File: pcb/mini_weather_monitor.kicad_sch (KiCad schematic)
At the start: 25 parts, among them J1 Conn_01x02, Q1 IRLML6402, U2 4.0inch_SPI_MSP4021, U2_BME280 module_bme280, U3_BH1750 module_bh1750

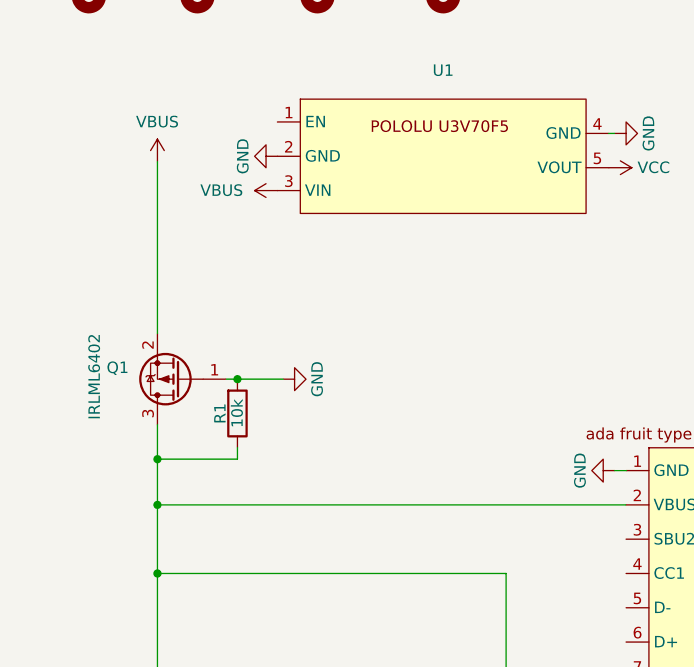
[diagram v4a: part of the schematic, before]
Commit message: fixing mosfet setup, also updating for day of the week length
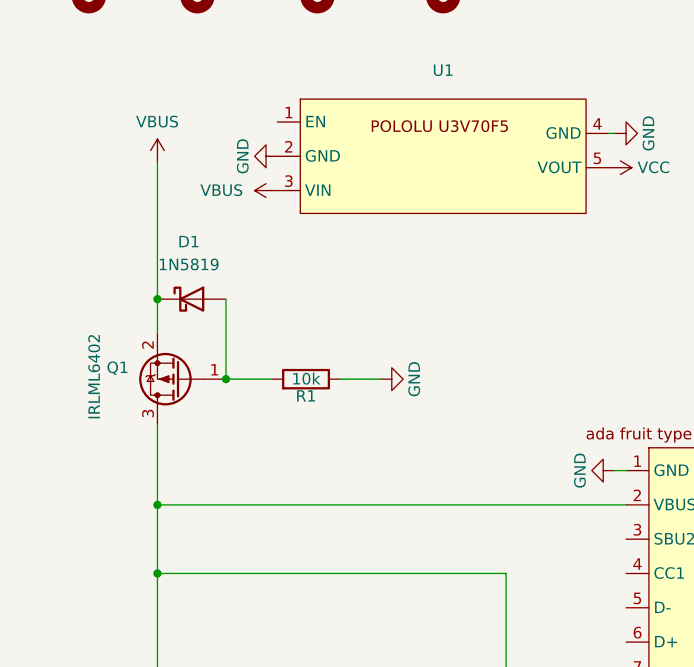
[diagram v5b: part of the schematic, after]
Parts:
- added D1: 1N5819, Diode_SMD:D_SOD-123, symbol Diode:1N5819
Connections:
- net GND: now also R1.1; no longer Q1.1 (G), R1.2
- net VBUS: now also D1.1 (K)
- net at Q1.3 (D), adafruit_type_c_breakout_rev_b1.2 (VBUS), adafruit_type_c_vertical_breakout1.10 (VBUS)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: no longer R1.1
- new net: D1.2 (A), Q1.1 (G), R1.2
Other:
- moved on the sheet: R1
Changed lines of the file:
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@@
+	)
+	(junction
+		(at 27.94 58.42)
+		(diameter 0)
+		(color 0 0 0 0)
 	)
 	(junction
@@
 	)
 	(junction
-		(at 27.94 76.2)
-		(diameter 0)
-		(color 0 0 0 0)
-	)
-	(junction
 		(at 253.365 91.44)
 		(diameter 0)
@@
 	)
 	(junction
+		(at 35.56 67.31)
+		(diameter 0)
+		(color 0 0 0 0)
+	)
+	(junction
 		(at 100.33 117.475)
 		(diameter 0)
@@
 	)
 	(junction
-		(at 36.83 67.31)
-		(diameter 0)
-		(color 0 0 0 0)
-	)
-	(junction
 		(at 196.85 55.245)
 		(diameter 0)
@@
 	(wire
 		(pts
-			(xy 27.94 43.18) (xy 27.94 62.23)
+			(xy 27.94 43.18) (xy 27.94 58.42)
 		)
 		(stroke
@@
 	(wire
 		(pts
+			(xy 35.56 58.42) (xy 35.56 67.31)
+		)
+		(stroke
+			(width 0)
+			(type default)
+		)
+	)
+	(wire
+		(pts
 			(xy 182.88 73.025) (xy 182.88 102.235)
 		)
@@
 	(wire
 		(pts
-			(xy 27.94 72.39) (xy 27.94 76.2)
+			(xy 27.94 72.39) (xy 27.94 81.28)
 		)
 		(stroke
@@
 	(wire
 		(pts
-			(xy 41.91 67.31) (xy 36.83 67.31)
-		)
-		(stroke
-			(width 0)
-			(type default)
-		)
-	)
-	(wire
-		(pts
 			(xy 248.285 35.56) (xy 248.285 77.47)
 		)
@@
 	(wire
 		(pts
-			(xy 36.83 67.31) (xy 35.56 67.31)
+			(xy 35.56 67.31) (xy 40.64 67.31)
 		)
 		(stroke
@@
 	(wire
 		(pts
+			(xy 27.94 58.42) (xy 27.94 62.23)
+		)
+		(stroke
+			(width 0)
+			(type default)
+		)
+	)
+	(wire
+		(pts
 			(xy 190.5 97.155) (xy 194.31 97.155)
 		)
@@
 	(wire
 		(pts
-			(xy 27.94 76.2) (xy 27.94 81.28)
-		)
-		(stroke
-			(width 0)
-			(type default)
-		)
-	)
-	(wire
-		(pts
 			(xy 205.105 60.325) (xy 179.07 60.325)
 		)
@@
 	(wire
 		(pts
-			(xy 36.83 76.2) (xy 27.94 76.2)
-		)
-		(stroke
-			(width 0)
-			(type default)
-		)
-	)
-	(wire
-		(pts
 			(xy 121.92 81.915) (xy 125.73 81.915)
 		)
@@
 	(wire
 		(pts
-			(xy 36.83 74.93) (xy 36.83 76.2)
-		)
-		(stroke
-			(width 0)
-			(type default)
-		)
-	)
-	(wire
-		(pts
 			(xy 156.21 46.355) (xy 158.75 46.355)
 		)
@@
 		(pts
 			(xy 95.885 112.395) (xy 100.33 112.395)
+		)
+		(stroke
+			(width 0)
+			(type default)
+		)
+	)
+	(wire
+		(pts
+			(xy 48.26 67.31) (xy 52.705 67.31)
 		)
 		(stroke
@@
 	(symbol
 		(lib_id "power:GND")
-		(at 41.91 67.31 90)
+		(at 52.705 67.31 90)
 		(unit 1)
 		(exclude_from_sim no)
@@
 		(dnp no)
 		(property "Reference" "#PWR015"
-			(at 48.26 67.31 0)
+			(at 59.055 67.31 0)
 			(effects
 				(font
@@
 		)
 		(property "Value" "GND"
-			(at 45.72 67.31 0)
+			(at 56.515 67.31 0)
 			(effects
 				(font
@@
 		)
 		(property "Footprint" ""
-			(at 41.91 67.31 0)
+			(at 52.705 67.31 0)
 			(effects
 				(font
@@
 		)
 		(property "Datasheet" ""
-			(at 41.91 67.31 0)
+			(at 52.705 67.31 0)
 			(effects
 				(font
@@
 		)
 		(property "Description" ""
-			(at 41.91 67.31 0)
+			(at 52.705 67.31 0)
 			(effects
 				(font
@@
 	(symbol
 		(lib_id "Device:R")
-		(at 36.83 71.12 0)
+		(at 44.45 67.31 270)
 		(mirror x)
 		(unit 1)
@@
 		(dnp no)
 		(property "Reference" "R1"
-			(at 34.925 71.12 90)
+			(at 44.45 69.215 90)
 			(effects
 				(font
@@
 		)
 		(property "Value" "10k"
-			(at 36.83 71.12 90)
+			(at 44.45 67.31 90)
 			(effects
 				(font
@@
 		)
 		(property "Footprint" "Resistor_SMD:R_1206_3216Metric"
-			(at 35.052 71.12 90)
+			(at 44.45 69.088 90)
 			(effects
 				(font
@@
 		)
 		(property "Datasheet" "~"
-			(at 36.83 71.12 0)
+			(at 44.45 67.31 0)
 			(effects
 				(font
@@
 		)
 		(property "Description" "Resistor"
-			(at 36.83 71.12 0)
+			(at 44.45 67.31 0)
 			(effects
 				(font
@@
 					(unit 1)
 				)
+			)
+		)
+	)
+	(symbol
+		(lib_id "Diode:1N5819")
+		(at 31.75 58.42 0)
+		(unit 1)
+		(exclude_from_sim no)
+		(in_bom yes)
+		(on_board yes)
+		(dnp no)
+		(fields_autoplaced yes)
+		(property "Reference" "D1"
+			(at 31.4325 52.07 0)
+			(effects
+				(font
+					(size 1.27 1.27)
+				)
+			)
+		)
+		(property "Value" "1N5819"
+			(at 31.4325 54.61 0)
+			(effects
+				(font
+					(size 1.27 1.27)
+				)
+			)
+		)
+		(property "Footprint" "Diode_SMD:D_SOD-123"
+			(at 31.75 62.865 0)
+			(effects
+				(font
+					(size 1.27 1.27)
+				)
+				(hide yes)
+			)
+		)
+		(property "Datasheet" "http://www.vishay.com/docs/88525/1n5817.pdf"
+			(at 31.75 58.42 0)
+			(effects
+				(font
+					(size 1.27 1.27)
+				)
+				(hide yes)
+			)
+		)
+		(property "Description" "40V 1A Schottky Barrier Rectifier Diode, DO-41"
+			(at 31.75 58.42 0)
+			(effects
+				(font
+					(size 1.27 1.27)
+				)
+				(hide yes)
+			)
+		)
+		(pin "1"
+		)
+		(pin "2"
+		)
+		(instances
+			(project "mini_weather_monitor"
+				(path "/e63e39d7-6ac0-4ffd-8aa3-1841a4541b55"
+					(reference "D1")
+					(unit 1)
+				)

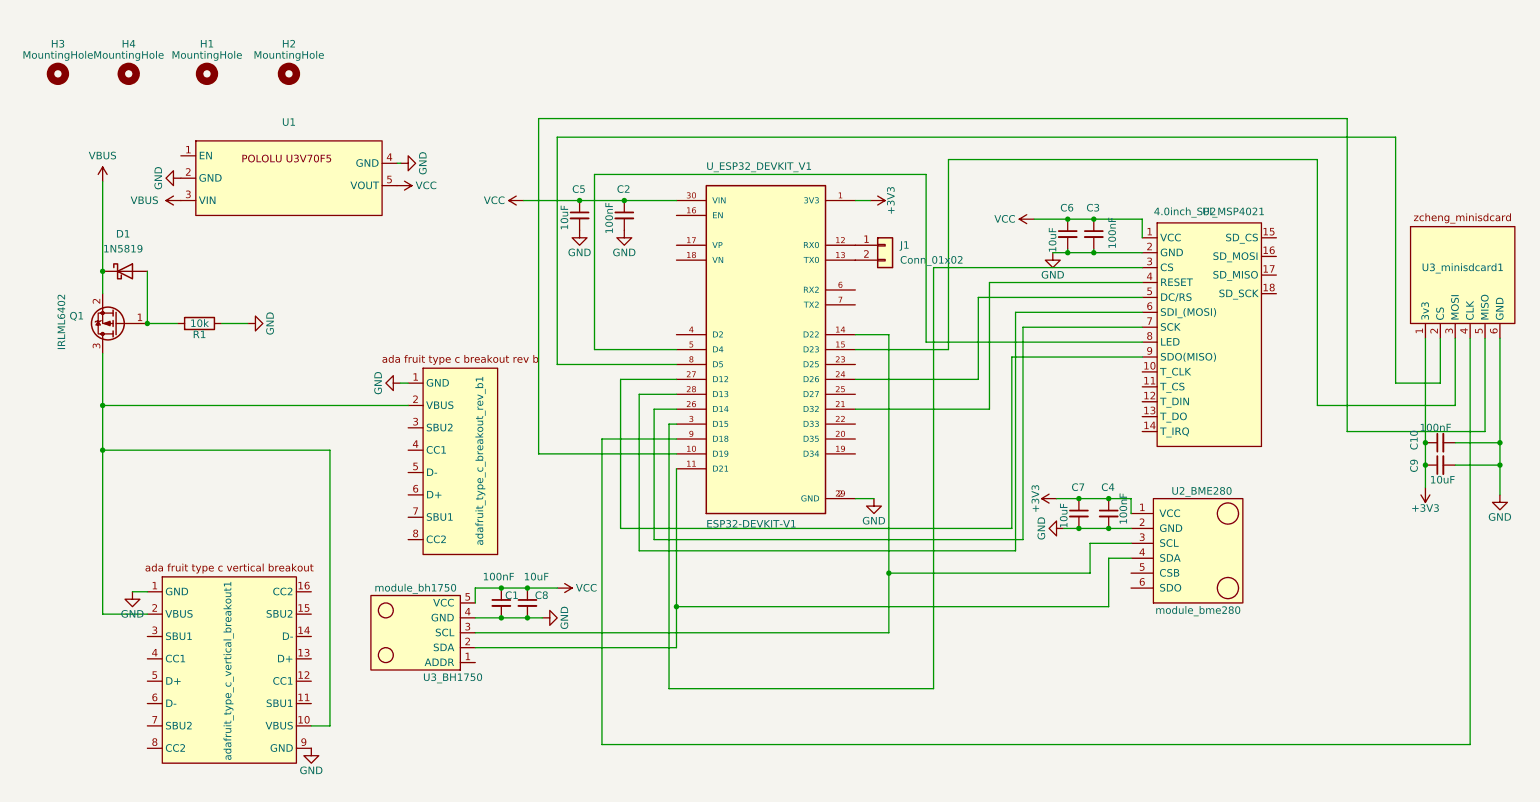
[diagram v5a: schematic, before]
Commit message: adding passthrough
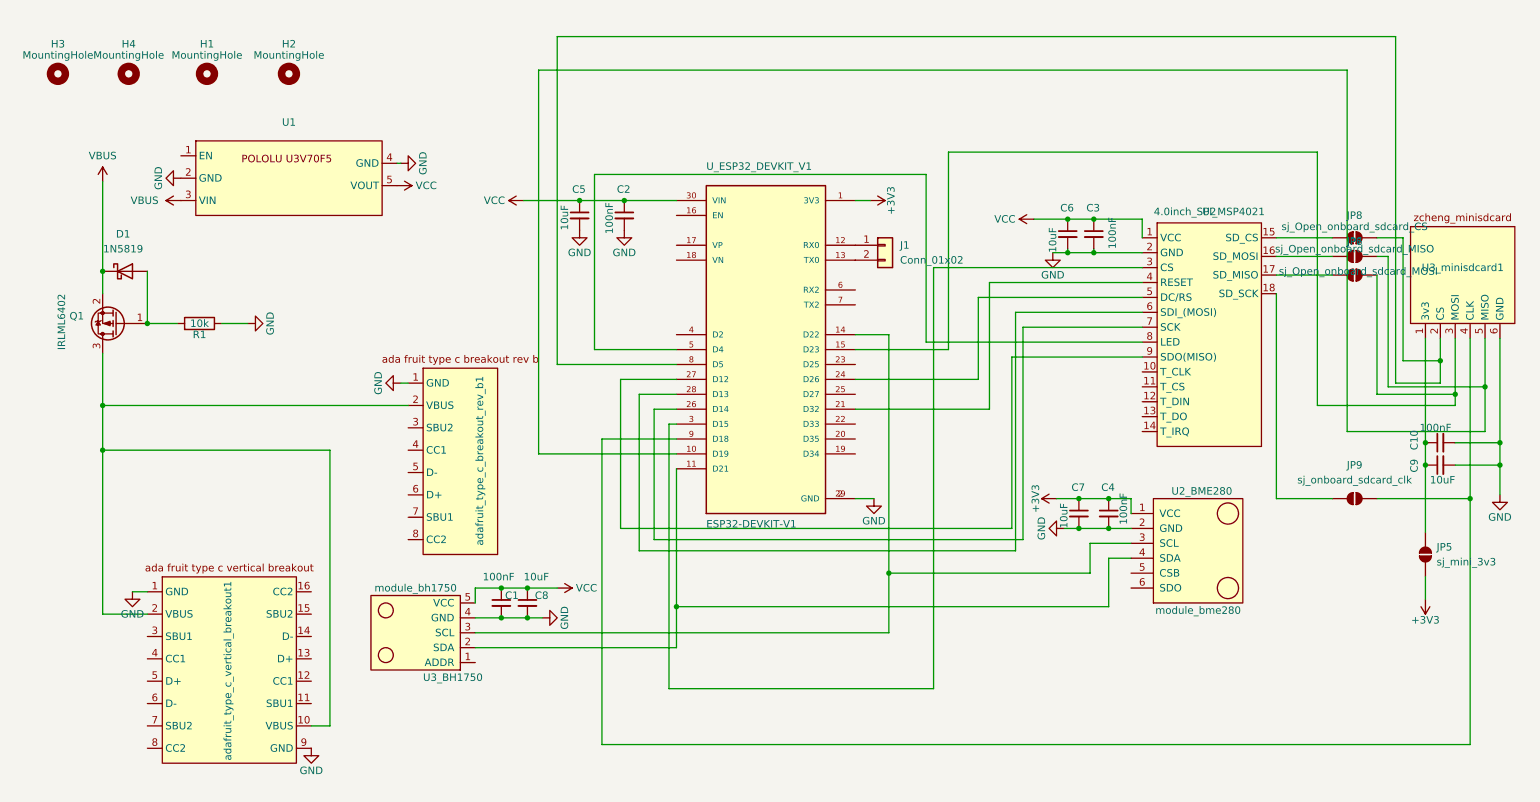
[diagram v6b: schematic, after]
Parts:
- added JP5: sj_mini_3v3, Jumper:SolderJumper-2_P1.3mm_Open_RoundedPad1.0x1.5mm, symbol Jumper:SolderJumper_2_Open
- added JP6: sj_Open_onboard_sdcard_MOSI, Jumper:SolderJumper-2_P1.3mm_Open_RoundedPad1.0x1.5mm, symbol Jumper:SolderJumper_2_Open
- added JP7: sj_Open_onboard_sdcard_MISO, Jumper:SolderJumper-2_P1.3mm_Open_RoundedPad1.0x1.5mm, symbol Jumper:SolderJumper_2_Open
- added JP8: sj_Open_onboard_sdcard_CS, Jumper:SolderJumper-2_P1.3mm_Open_RoundedPad1.0x1.5mm, symbol Jumper:SolderJumper_2_Open
- added JP9: sj_onboard_sdcard_clk, Jumper:SolderJumper-2_P1.3mm_Open_RoundedPad1.0x1.5mm, symbol Jumper:SolderJumper_2_Open
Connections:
- net +3V3: now also JP5.1 (A); no longer C10.1, C9.1, U3_minisdcard1.1 (3v3)
- net at U2.15 (SD_CS): now also JP8.1 (A)
- net at U2.16 (SD_MOSI): now also JP6.1 (A)
- net at U2.17 (SD_MISO): now also JP7.1 (A)
- net at U2.18 (SD_SCK): now also JP9.1 (A)
- net at U3_minisdcard1.5 (MISO), U_ESP32_DEVKIT_V1.10 (D19): now also JP6.2 (B)
- net at U3_minisdcard1.3 (MOSI), U_ESP32_DEVKIT_V1.15 (D23): now also JP7.2 (B)
- net at U3_minisdcard1.2 (CS), U_ESP32_DEVKIT_V1.8 (D5): now also JP8.2 (B)
- net at U3_minisdcard1.4 (CLK), U_ESP32_DEVKIT_V1.9 (D18): now also JP9.2 (B)
- new net: C10.1, C9.1, JP5.2 (B), U3_minisdcard1.1 (3v3)

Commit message: slight retrace
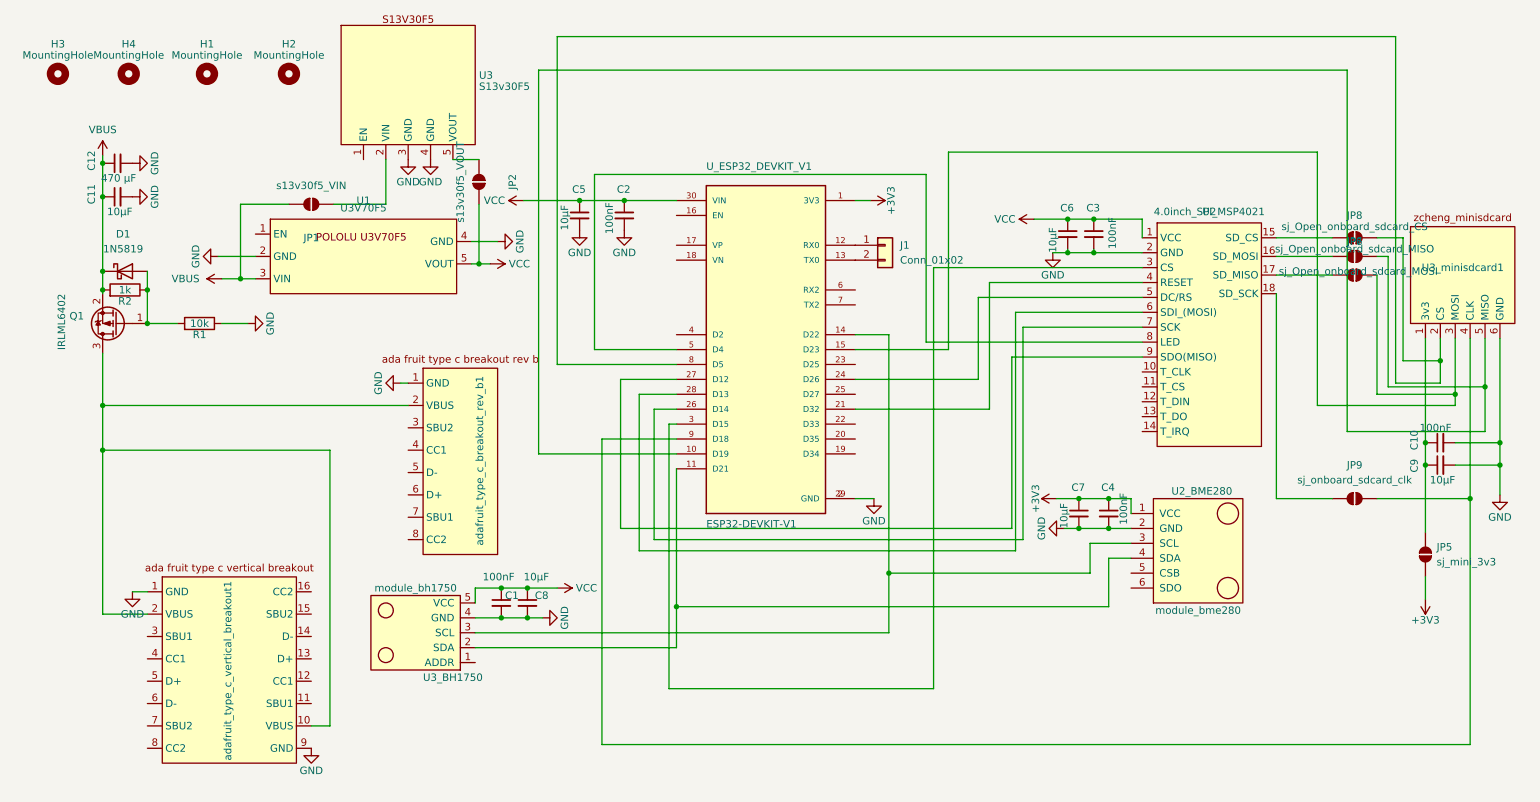
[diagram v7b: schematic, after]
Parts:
- added C11: 10µF, Capacitor_SMD:C_1206_3216Metric_Pad1.33x1.80mm_HandSolder, symbol Device:C_Small
- added C12: 470 µF, Capacitor_SMD:C_1206_3216Metric_Pad1.33x1.80mm_HandSolder, symbol Device:C_Small
- added JP1: s13v30f5_VIN, Jumper:SolderJumper-2_P1.3mm_Open_RoundedPad1.0x1.5mm, symbol Jumper:SolderJumper_2_Open
- added JP2: s13v30f5_VOUT, Jumper:SolderJumper-2_P1.3mm_Open_RoundedPad1.0x1.5mm, symbol Jumper:SolderJumper_2_Open
- added R2: 1k, Resistor_SMD:R_1206_3216Metric, symbol Device:R
- added U3: S13v30F5, boost_converter:pololu S13V30F5 step up step down, symbol boost_converter:pololu_S13V30F5
- C5, C6, C7, C8, C9: value 10uF -> 10µF
- U1: value ~ -> U3V70F5
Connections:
- net GND: now also C11.2, C12.2, U3.3 (GND), U3.4 (GND)
- net VBUS: now also C11.1, C12.1, JP1.2 (B), R2.2
- net VCC: now also JP2.2 (B)
- net at D1.2 (A), Q1.1 (G), R1.2: now also R2.1
- new net: JP1.1 (A), U3.2 (VIN)
- new net: JP2.1 (A), U3.5 (VOUT)
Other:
- moved on the sheet: U1
